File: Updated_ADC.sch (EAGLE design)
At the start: 20 parts, among them U1 AD5254BRUZ1, U2 ADS1256IDBR, U3 AD5254BRUZ1, U4 ATMEGA328P_VQFNVQFN, Y1 8MHz, Y2 16MHz

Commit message: Version 2_UPDATED_ADC
Added in voltage regulators, power and programming headers, and bypass capacitors
TODO: Still need to add in SD card reader circuitry.

CHECK: Do we need to set AGND on the ADC to the sensor ground? Is the 0.5V regulator going to produce a steady reference voltage? What is the voltage for the strain gauges (UPDATE R2 VALUE WHEN WE KNOW)?
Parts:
- removed U3: AD5254BRUZ1, AD5254 Digital Potentiometer:AD5254BRUZ1
- added +3V_BYP, +5V_BYP, ADC_BYP_A, ADC_BYP_D, GAUGE_BYP, MEGA_BYP, POT_BYP, POWER_BYP, PROG_BYP, VREF_BYP: 22uF, resistor:C-USC1206
- added 3V_REG, 5V_REG, GAUGE_REG: V_REG_317SMD, SparkFun-IC-Power:V_REG_317SMD
- added 3V_REG_R1, 5V_REG_R1, GAUGE_REG_R1: 240, rcl:R-US_R1206
- added 3V_REG_R2: 390, rcl:R-US_R1206
- added 5V_REG_R2: 720, rcl:R-US_R1206
- added B1_R1, B2_R1, B3_R1, B4_R1: 350, resistor:R-US_R1206
- added B1_R2, B2_R2, B3_R2, B4_R2: 370, resistor:R-US_R1206
- added B1_R3, B2_R3, B3_R3, B4_R3: 5k, resistor:R-US_R1206
- added GAUGE_REG_R2: ??, rcl:R-US_R1206
- added ICSP: (no value), SparkFun-Connectors:CONN_03X2FEMALE
- added MEGA_RESET_R1: 10k, resistor:R-US_M1206
- added VREF_R1: 240, resistor:R-US_R1206
- added VREF_R2: 27, resistor:R-US_R1206
- added X5: (no value), con-phoenix-254:MPT2
- renumbered U1 to POT
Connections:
- removed net +VREF: U2B.VREFP
- removed net -VREF: U2B.VREFN
- removed net N$1: U2B.AGND, U2B.DGND
- new net +3V: +3V_BYP.1, 3V_REG.OUT
- new net N$12: 3V_REG.ADJ, 3V_REG_R1.1, 3V_REG_R2.2
- new net N$20: GAUGE_REG.ADJ, GAUGE_REG_R1.1, GAUGE_REG_R2.2
- new net N$8: 5V_REG.ADJ, 5V_REG_R1.1, 5V_REG_R2.2
- new net POT1: B1_R3.2, POT.B0
- new net POT2: B2_R3.2, POT.B1
- new net POT3: B3_R3.2, POT.B2
- new net POT4: B4_R3.2, POT.B3
- new net VIN: 3V_REG.IN, 5V_REG.IN, GAUGE_REG.IN, POWER_BYP.1, X5-1.1
- new net VREF: U2B.VREFP, VREF_BYP.1, VREF_R1.1, VREF_R2.2
- net +5V: now also +5V_BYP.1, 5V_REG.OUT, ADC_BYP_A.1, ADC_BYP_D.1, ICSP.2, MEGA_BYP.1, MEGA_RESET_R1.2, POT_BYP.1, PROG_BYP.1, VREF_R1.2; no longer U3.VDD
- net +V: now also B1_R1.1, B2_R1.1, B3_R1.1, B4_R1.1, GAUGE_BYP.1, GAUGE_REG.OUT; no longer POT.B0, POT.B2, U3.B0, U3.B2
- net B1_+: now also B1_R1.2; no longer POT.W0
- net B1_-: now also B1_R2.1, POT.W0; no longer POT.B1
- net B2_+: now also B2_R1.2; no longer POT.W2
- net B2_-: now also B2_R2.1, POT.W1; no longer POT.B3
- net B3_+: now also B3_R1.2; no longer U3.W0
- net B3_-: now also B3_R2.1, POT.W2; no longer U3.B1
- net B4_+: now also B4_R1.2; no longer U3.W2
- net B4_-: now also B4_R2.1, POT.W3; no longer U3.B3
- net GND: now also +3V_BYP.2, +5V_BYP.2, 3V_REG_R2.1, 5V_REG_R2.1, ADC_BYP_A.2, ADC_BYP_D.2, B1_R2.2, B1_R3.1, B2_R2.2, B2_R3.1, B3_R2.2, B3_R3.1, B4_R2.2, B4_R3.1, GAUGE_BYP.2, GAUGE_REG_R2.1, ICSP.6, MEGA_BYP.2, POT_BYP.2, POWER_BYP.2, PROG_BYP.2, U2B.AGND, U2B.DGND, U2B.VREFN, VREF_BYP.2, VREF_R2.1, X5-2.1; no longer POT.W1, POT.W3, U3.DGND, U3.VSS, U3.W1, U3.W3
- net MISO: now also ICSP.1
- net MOSI: now also ICSP.4
- net POT_A0: no longer U3.AD0
- net POT_A1: no longer U3.AD1
- net RESET: now also ICSP.5, MEGA_RESET_R1.1, U4.PC6(/RESET)
- net SCK: now also ICSP.3
- net SCL: no longer U3.SCL
- net SDA: no longer U3.SDA

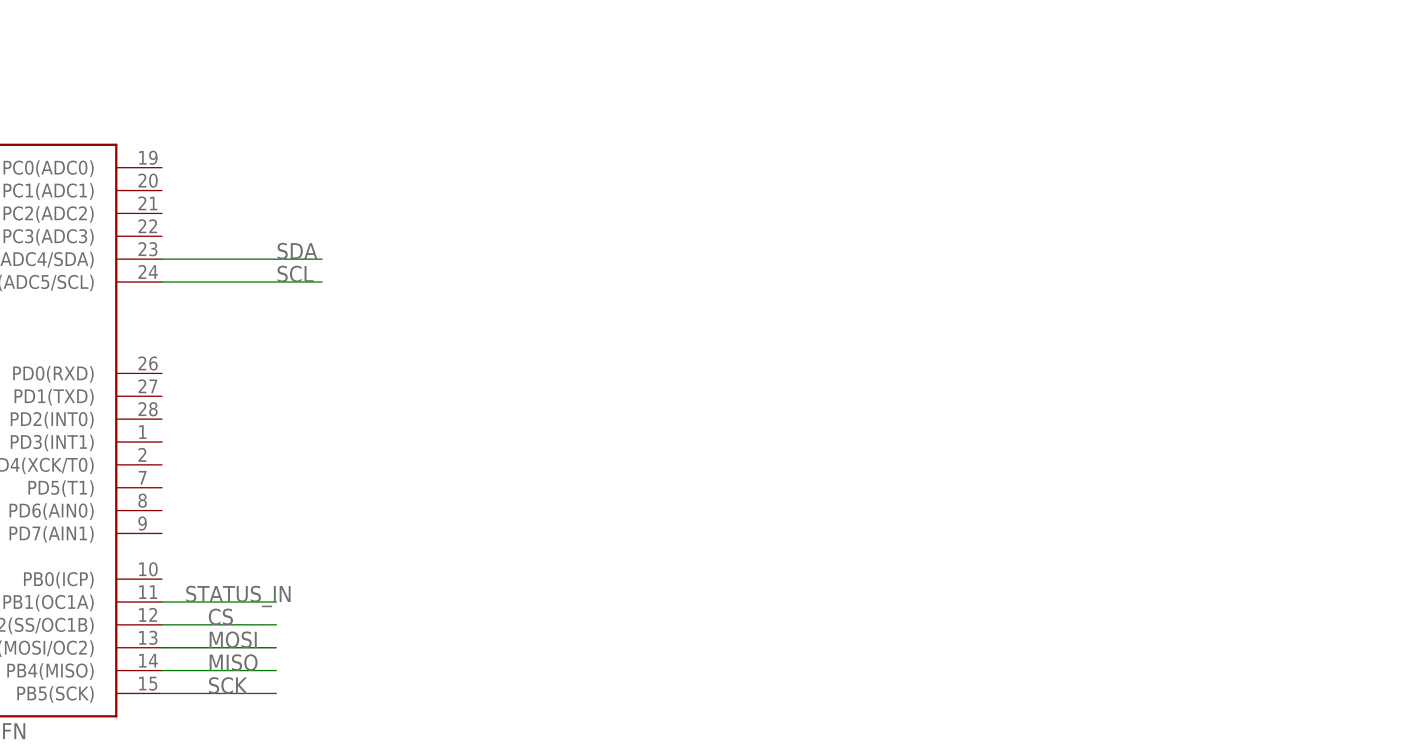
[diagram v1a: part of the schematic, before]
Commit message: Added SD Card reader
TODO: Verify if we need to use 3V3 or 5V for the SD card. If it's 3V, then we need to add in a level shifter between ATMEGA and the card.
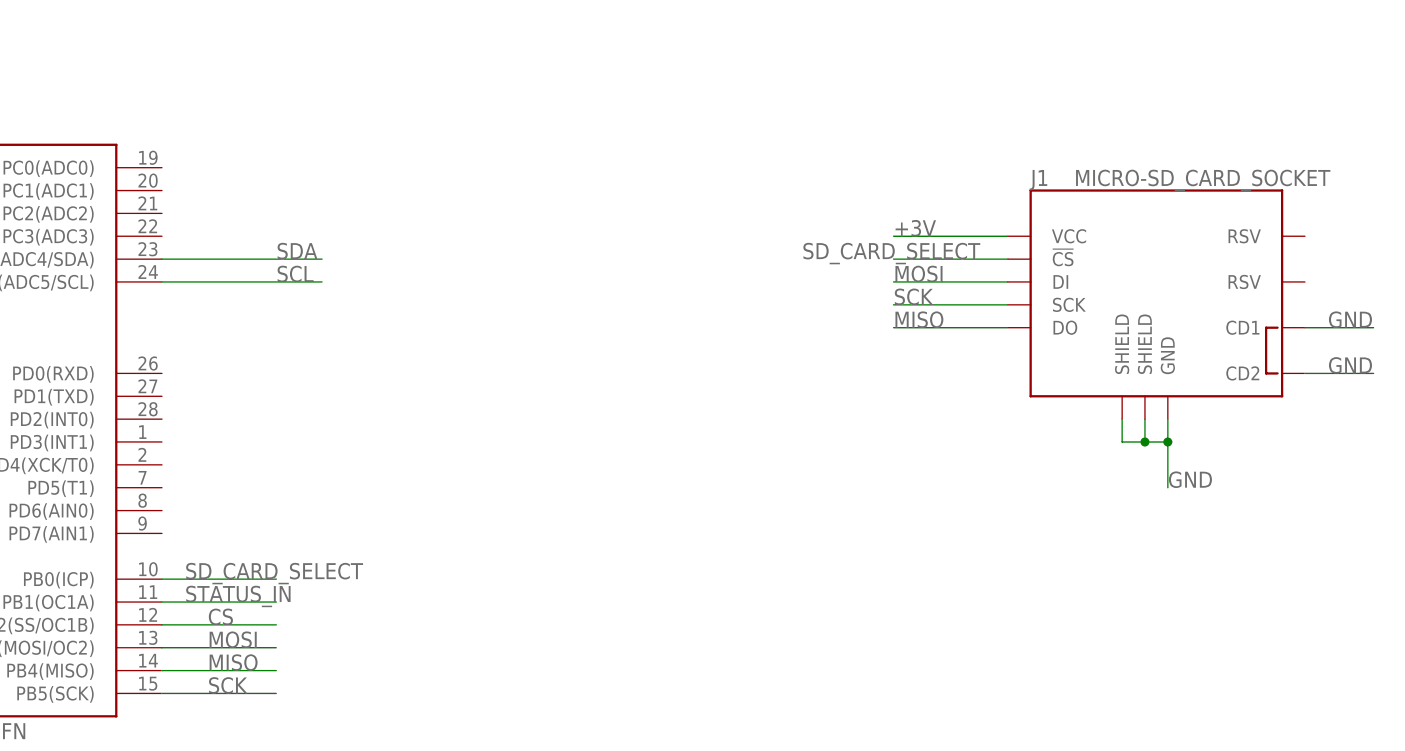
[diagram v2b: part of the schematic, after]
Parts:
- added J1: MICRO-SD_CARD_SOCKET, SparkFun-Connectors:MICRO-SD_CARD_SOCKET
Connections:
- new net SD_CARD_SELECT: J1.!CS, U4.PB0(ICP)
- net +3V: now also J1.VCC
- net GND: now also J1.CD1, J1.CD2, J1.GND, J1.SHIELD@1, J1.SHIELD@3
- net MISO: now also J1.DO
- net MOSI: now also J1.DI
- net SCK: now also J1.SCK
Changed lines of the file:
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@@
 <part name="VREF_R2" library="resistor" library_urn="urn:adsk.eagle:library:348" deviceset="R-US_" device="R1206" package3d_urn="urn:adsk.eagle:package:23540/2" value="27"/>
 <part name="VREF_BYP" library="resistor" library_urn="urn:adsk.eagle:library:348" deviceset="C-US" device="C1206" package3d_urn="urn:adsk.eagle:package:23618/2" value="22uF"/>
+<part name="J1" library="SparkFun-Connectors" library_urn="urn:adsk.eagle:library:513" deviceset="MICRO-SD_CARD_SOCKET" device="" package3d_urn="urn:adsk.eagle:package:38283/1"/>
 </parts>
 <sheets>
@@
 <instance part="VREF_R2" gate="G$1" x="226.06" y="195.58" rot="R90"/>
 <instance part="VREF_BYP" gate="G$1" x="238.76" y="195.58"/>
+<instance part="J1" gate="1" x="581.66" y="-35.56"/>
 </instances>
 <busses>
@@
 <junction x="226.06" y="187.96"/>
 </segment>
+<segment>
+<pinref part="J1" gate="1" pin="GND"/>
+<wire x1="584.2" y1="-50.8" x2="584.2" y2="-53.34" width="0.1524" layer="91"/>
+<label x="584.2" y="-58.42" size="1.778" layer="95"/>
+<pinref part="J1" gate="1" pin="SHIELD@3"/>
+<wire x1="584.2" y1="-53.34" x2="584.2" y2="-58.42" width="0.1524" layer="91"/>
+<wire x1="581.66" y1="-50.8" x2="581.66" y2="-53.34" width="0.1524" layer="91"/>
+<wire x1="581.66" y1="-53.34" x2="584.2" y2="-53.34" width="0.1524" layer="91"/>
+<junction x="584.2" y="-53.34"/>
+<pinref part="J1" gate="1" pin="SHIELD@1"/>
+<wire x1="579.12" y1="-50.8" x2="579.12" y2="-53.34" width="0.1524" layer="91"/>
+<wire x1="579.12" y1="-53.34" x2="581.66" y2="-53.34" width="0.1524" layer="91"/>
+<junction x="581.66" y="-53.34"/>
+</segment>
+<segment>
+<pinref part="J1" gate="1" pin="CD1"/>
+<wire x1="599.44" y1="-40.64" x2="607.06" y2="-40.64" width="0.1524" layer="91"/>
+<label x="601.98" y="-40.64" size="1.778" layer="95"/>
+</segment>
+<segment>
+<pinref part="J1" gate="1" pin="CD2"/>
+<wire x1="599.44" y1="-45.72" x2="607.06" y2="-45.72" width="0.1524" layer="91"/>
+<label x="601.98" y="-45.72" size="1.778" layer="95"/>
+</segment>
 </net>
 <net name="SDA" class="0">
@@
 <label x="431.8" y="-132.08" size="1.778" layer="95"/>
 </segment>
+<segment>
+<pinref part="J1" gate="1" pin="SCK"/>
+<wire x1="566.42" y1="-38.1" x2="553.72" y2="-38.1" width="0.1524" layer="91"/>
+<label x="553.72" y="-38.1" size="1.778" layer="95"/>
+</segment>
 </net>
 <net name="MOSI" class="0">
@@
 <label x="457.2" y="-132.08" size="1.778" layer="95"/>
 </segment>
+<segment>
+<pinref part="J1" gate="1" pin="DI"/>
+<wire x1="566.42" y1="-35.56" x2="553.72" y2="-35.56" width="0.1524" layer="91"/>
+<label x="553.72" y="-35.56" size="1.778" layer="95"/>
+</segment>
 </net>
 <net name="MISO" class="0">
@@
 <wire x1="439.42" y1="-129.54" x2="431.8" y2="-129.54" width="0.1524" layer="91"/>
 <label x="431.8" y="-129.54" size="1.778" layer="95"/>
+</segment>
+<segment>
+<pinref part="J1" gate="1" pin="DO"/>
+<wire x1="566.42" y1="-40.64" x2="553.72" y2="-40.64" width="0.1524" layer="91"/>
+<label x="553.72" y="-40.64" size="1.778" layer="95"/>
 </segment>
 </net>
@@
 <wire x1="147.32" y1="218.44" x2="144.78" y2="218.44" width="0.1524" layer="91"/>
 </segment>
+<segment>
+<pinref part="J1" gate="1" pin="VCC"/>
+<wire x1="566.42" y1="-30.48" x2="553.72" y2="-30.48" width="0.1524" layer="91"/>
+<label x="553.72" y="-30.48" size="1.778" layer="95"/>
+</segment>
 </net>
 <net name="N$20" class="0">
@@
 </segment>
 </net>
+<net name="SD_CARD_SELECT" class="0">
+<segment>
+<pinref part="U4" gate="G$1" pin="PB0(ICP)"/>
+<wire x1="472.44" y1="-68.58" x2="485.14" y2="-68.58" width="0.1524" layer="91"/>
+<label x="474.98" y="-68.58" size="1.778" layer="95"/>
+</segment>
+<segment>
+<pinref part="J1" gate="1" pin="!CS"/>
+<wire x1="566.42" y1="-33.02" x2="553.72" y2="-33.02" width="0.1524" layer="91"/>
+<label x="543.56" y="-33.02" size="1.778" layer="95"/>
+</segment>
+</net>

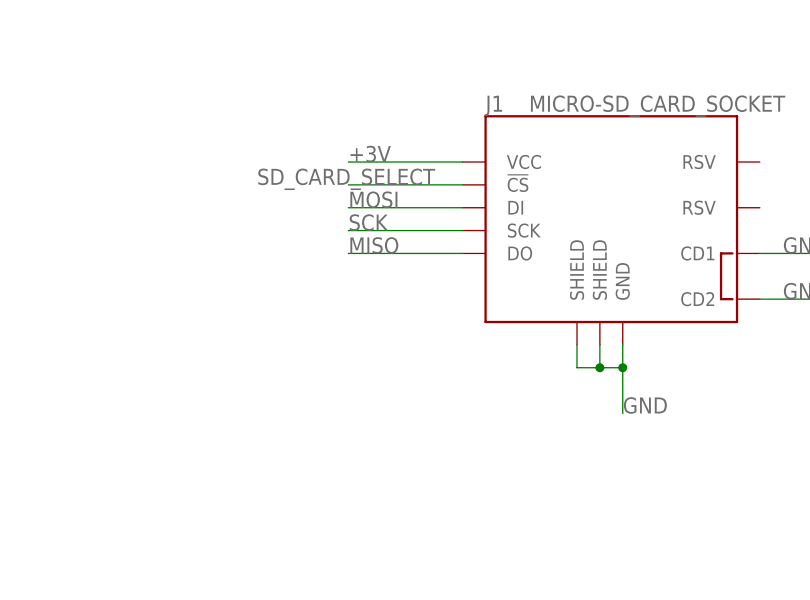
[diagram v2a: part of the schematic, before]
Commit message: Added SD Card
Forgot to add bypass cap to the SD card reader
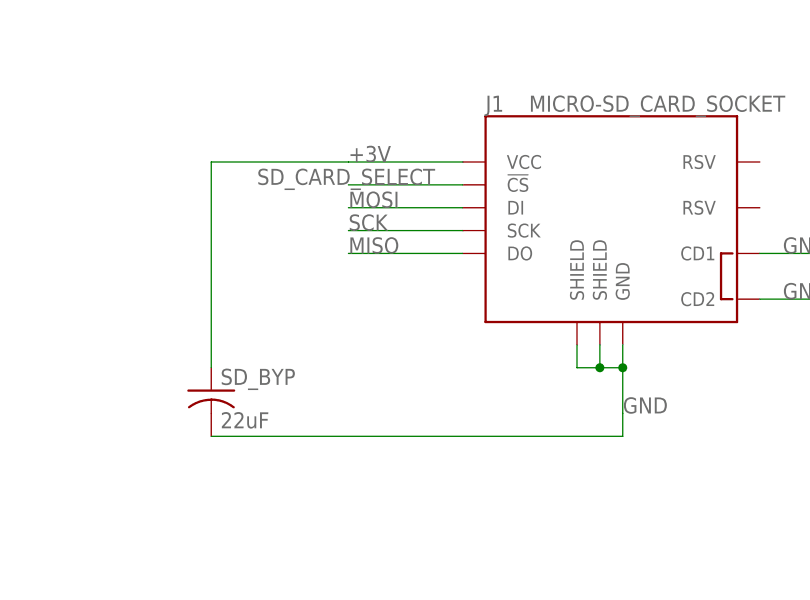
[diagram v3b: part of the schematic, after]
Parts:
- added SD_BYP: 22uF, resistor:C-USC1206
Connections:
- net +3V: now also SD_BYP.1
- net GND: now also SD_BYP.2
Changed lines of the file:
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@@
 <part name="VREF_BYP" library="resistor" library_urn="urn:adsk.eagle:library:348" deviceset="C-US" device="C1206" package3d_urn="urn:adsk.eagle:package:23618/2" value="22uF"/>
 <part name="J1" library="SparkFun-Connectors" library_urn="urn:adsk.eagle:library:513" deviceset="MICRO-SD_CARD_SOCKET" device="" package3d_urn="urn:adsk.eagle:package:38283/1"/>
+<part name="SD_BYP" library="resistor" library_urn="urn:adsk.eagle:library:348" deviceset="C-US" device="C1206" package3d_urn="urn:adsk.eagle:package:23618/2" value="22uF"/>
 </parts>
 <sheets>
@@
 <instance part="VREF_BYP" gate="G$1" x="238.76" y="195.58"/>
 <instance part="J1" gate="1" x="581.66" y="-35.56"/>
+<instance part="SD_BYP" gate="G$1" x="538.48" y="-55.88"/>
 </instances>
 <busses>
@@
 <wire x1="579.12" y1="-53.34" x2="581.66" y2="-53.34" width="0.1524" layer="91"/>
 <junction x="581.66" y="-53.34"/>
+<pinref part="SD_BYP" gate="G$1" pin="2"/>
+<wire x1="538.48" y1="-60.96" x2="584.2" y2="-60.96" width="0.1524" layer="91"/>
+<wire x1="584.2" y1="-60.96" x2="584.2" y2="-58.42" width="0.1524" layer="91"/>
 </segment>
 <segment>
@@
 <wire x1="566.42" y1="-30.48" x2="553.72" y2="-30.48" width="0.1524" layer="91"/>
 <label x="553.72" y="-30.48" size="1.778" layer="95"/>
-</segment>
-</net>
+<pinref part="SD_BYP" gate="G$1" pin="1"/>
+<wire x1="538.48" y1="-53.34" x2="538.48" y2="-30.48" width="0.1524" layer="91"/>
+<wire x1="538.48" y1="-30.48" x2="553.72" y2="-30.48" width="0.1524" layer="91"/>
+</segment>
+</net>
